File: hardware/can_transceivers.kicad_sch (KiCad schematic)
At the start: 0 parts

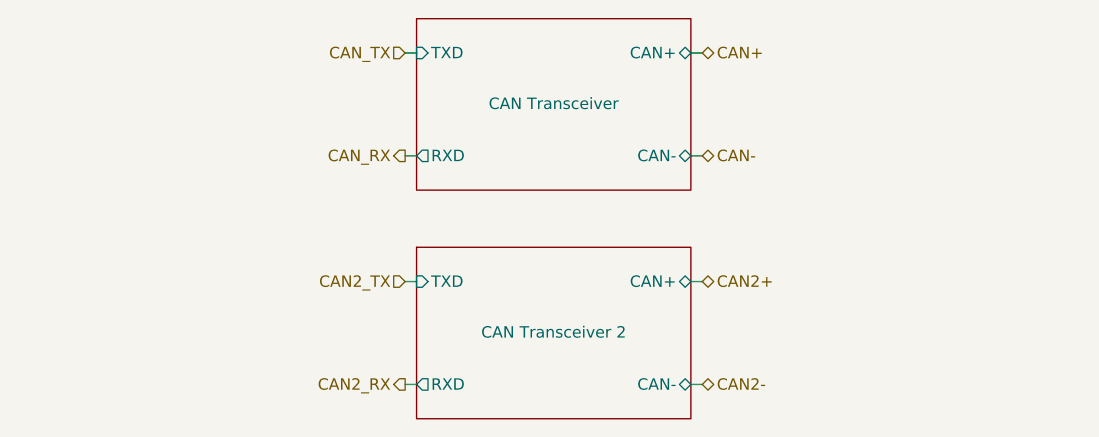
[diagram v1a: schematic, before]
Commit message: Improve the schematic
- add anti-aliasing filters
- rearrange the main connector signals
- improve the power filtering
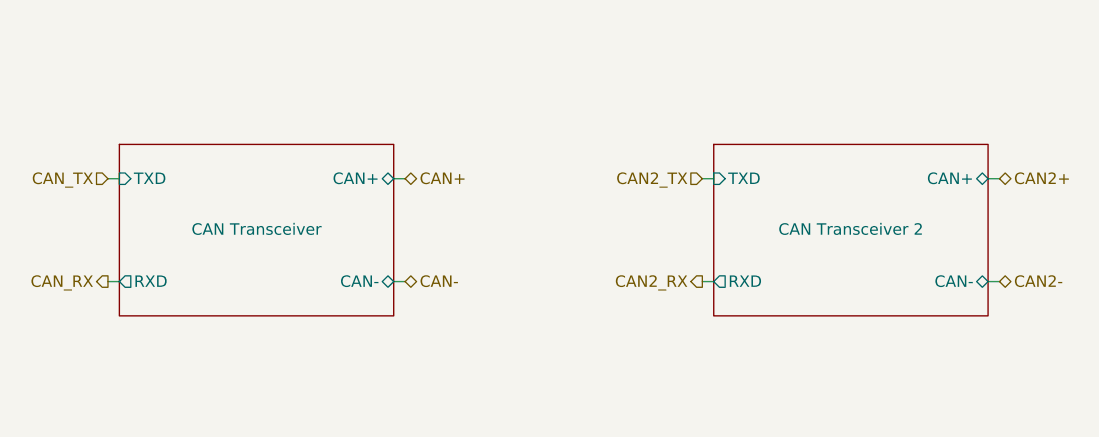
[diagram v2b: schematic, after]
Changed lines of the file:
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@@
     (comment 1 "Reviewer:")
   )
-  (wire (pts (xy 165.1 92.71) (xy 166.37 92.71))
+  (wire (pts (xy 132.08 106.68) (xy 133.35 106.68))
     (stroke (width 0) (type default))
   )
-  (wire (pts (xy 133.35 92.71) (xy 134.62 92.71))
+  (wire (pts (xy 100.33 106.68) (xy 101.6 106.68))
     (stroke (width 0) (type default))
   )
-  (wire (pts (xy 133.35 106.68) (xy 134.62 106.68))
+  (wire (pts (xy 166.37 95.25) (xy 167.64 95.25))
     (stroke (width 0) (type default))
   )
-  (wire (pts (xy 165.1 81.28) (xy 166.37 81.28))
+  (wire (pts (xy 132.08 95.25) (xy 133.35 95.25))
     (stroke (width 0) (type default))
   )
-  (wire (pts (xy 133.35 118.11) (xy 134.62 118.11))
+  (wire (pts (xy 166.37 106.68) (xy 167.64 106.68))
     (stroke (width 0) (type default))
   )
-  (wire (pts (xy 133.35 81.28) (xy 134.62 81.28))
+  (wire (pts (xy 100.33 95.25) (xy 101.6 95.25))
     (stroke (width 0) (type default))
   )
-  (wire (pts (xy 165.1 106.68) (xy 166.37 106.68))
+  (wire (pts (xy 198.12 95.25) (xy 199.39 95.25))
     (stroke (width 0) (type default))
   )
-  (wire (pts (xy 165.1 118.11) (xy 166.37 118.11))
+  (wire (pts (xy 198.12 106.68) (xy 199.39 106.68))
     (stroke (width 0) (type default))
   )
-  (hierarchical_label "CAN2_RX" (shape output) (at 133.35 118.11 180) (fields_autoplaced)
+  (hierarchical_label "CAN2_RX" (shape output) (at 166.37 106.68 180) (fields_autoplaced)
     (effects (font (size 1.27 1.27)) (justify right))
   )
-  (hierarchical_label "CAN2+" (shape bidirectional) (at 166.37 106.68 0) (fields_autoplaced)
+  (hierarchical_label "CAN2+" (shape bidirectional) (at 199.39 95.25 0) (fields_autoplaced)
     (effects (font (size 1.27 1.27)) (justify left))
   )
-  (hierarchical_label "CAN-" (shape bidirectional) (at 166.37 92.71 0) (fields_autoplaced)
+  (hierarchical_label "CAN-" (shape bidirectional) (at 133.35 106.68 0) (fields_autoplaced)
     (effects (font (size 1.27 1.27)) (justify left))
   )
-  (hierarchical_label "CAN2-" (shape bidirectional) (at 166.37 118.11 0) (fields_autoplaced)
+  (hierarchical_label "CAN2-" (shape bidirectional) (at 199.39 106.68 0) (fields_autoplaced)
     (effects (font (size 1.27 1.27)) (justify left))
   )
-  (hierarchical_label "CAN_RX" (shape output) (at 133.35 92.71 180) (fields_autoplaced)
+  (hierarchical_label "CAN_RX" (shape output) (at 100.33 106.68 180) (fields_autoplaced)
     (effects (font (size 1.27 1.27)) (justify right))
   )
-  (hierarchical_label "CAN2_TX" (shape input) (at 133.35 106.68 180) (fields_autoplaced)
+  (hierarchical_label "CAN2_TX" (shape input) (at 166.37 95.25 180) (fields_autoplaced)
     (effects (font (size 1.27 1.27)) (justify right))
   )
-  (hierarchical_label "CAN_TX" (shape input) (at 133.35 81.28 180) (fields_autoplaced)
+  (hierarchical_label "CAN_TX" (shape input) (at 100.33 95.25 180) (fields_autoplaced)
     (effects (font (size 1.27 1.27)) (justify right))
   )
-  (hierarchical_label "CAN+" (shape bidirectional) (at 166.37 81.28 0) (fields_autoplaced)
+  (hierarchical_label "CAN+" (shape bidirectional) (at 133.35 95.25 0) (fields_autoplaced)
     (effects (font (size 1.27 1.27)) (justify left))
   )
-  (sheet (at 134.62 77.47) (size 30.48 19.05)
+  (sheet (at 101.6 91.44) (size 30.48 19.05)
     (stroke (width 0.1524) (type solid))
     (fill (color 0 0 0 0.0000))
-    (property "Sheetname" "CAN Transceiver" (at 149.86 86.9184 0)
+    (property "Sheetname" "CAN Transceiver" (at 116.84 100.8884 0)
       (effects (font (size 1.27 1.27)))
     )
-    (property "Sheetfile" "can_transceiver.kicad_sch" (at 134.62 94.5646 0)
+    (property "Sheetfile" "can_transceiver.kicad_sch" (at 101.6 108.5346 0)
       (effects (font (size 1.27 1.27)) (justify left top) hide)
     )
-    (pin "RXD" output (at 134.62 92.71 180)
+    (pin "RXD" output (at 101.6 106.68 180)
       (effects (font (size 1.27 1.27)) (justify left))
     )
-    (pin "TXD" input (at 134.62 81.28 180)
+    (pin "TXD" input (at 101.6 95.25 180)
       (effects (font (size 1.27 1.27)) (justify left))
     )
-    (pin "CAN-" bidirectional (at 165.1 92.71 0)
+    (pin "CAN-" bidirectional (at 132.08 106.68 0)
       (effects (font (size 1.27 1.27)) (justify right))
     )
-    (pin "CAN+" bidirectional (at 165.1 81.28 0)
+    (pin "CAN+" bidirectional (at 132.08 95.25 0)
       (effects (font (size 1.27 1.27)) (justify right))
     )
@@
     )
   )
-  (sheet (at 134.62 102.87) (size 30.48 19.05)
+  (sheet (at 167.64 91.44) (size 30.48 19.05)
     (stroke (width 0.1524) (type solid))
     (fill (color 0 0 0 0.0000))
-    (property "Sheetname" "CAN Transceiver 2" (at 149.86 112.3184 0)
+    (property "Sheetname" "CAN Transceiver 2" (at 182.88 100.8884 0)
       (effects (font (size 1.27 1.27)))
     )
-    (property "Sheetfile" "can_transceiver.kicad_sch" (at 134.62 119.9646 0)
+    (property "Sheetfile" "can_transceiver.kicad_sch" (at 167.64 108.5346 0)
       (effects (font (size 1.27 1.27)) (justify left top) hide)
     )
-    (pin "RXD" output (at 134.62 118.11 180)
+    (pin "RXD" output (at 167.64 106.68 180)
       (effects (font (size 1.27 1.27)) (justify left))
     )
-    (pin "TXD" input (at 134.62 106.68 180)
+    (pin "TXD" input (at 167.64 95.25 180)
       (effects (font (size 1.27 1.27)) (justify left))
     )
-    (pin "CAN-" bidirectional (at 165.1 118.11 0)
+    (pin "CAN-" bidirectional (at 198.12 106.68 0)
       (effects (font (size 1.27 1.27)) (justify right))
     )
-    (pin "CAN+" bidirectional (at 165.1 106.68 0)
+    (pin "CAN+" bidirectional (at 198.12 95.25 0)
       (effects (font (size 1.27 1.27)) (justify right))
     )
